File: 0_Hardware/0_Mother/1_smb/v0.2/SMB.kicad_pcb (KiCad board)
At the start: 2 copper layers, 100 x 86 mm, 104 parts, among them IC1 MAX485, IC101 ATMEGA1284-A, IC2 DS2482-100S, J101 RJ45, J102 RTS_RESET, J103 ICSP, J104 SERIAL_REV, J202 USD_CONN, J401 HR911105_RJ45, P1 CONN_2, P101 I2C_CONN, P102 CONN_10X2, P103 CONN_5, P105 CONN_5, P107 CONN_3, P108 CONN_5, P109 CONN_3, P110 CONN_3, P112 CONN_3, P2 CONN_3, P3 CONN_3, P301 CONN_2, P4 CONN_3, P5 CONN_2, Q1 BSS84, SW101 SKQGAKE010, U1 DS1340, U201 ENC28J60, U202 LM1117IMP-3.3, U301 74HC08, U302 MP2562DS, U303 74HC08, X1 CRYSTAL, X101 20MHz, X201 25MHz

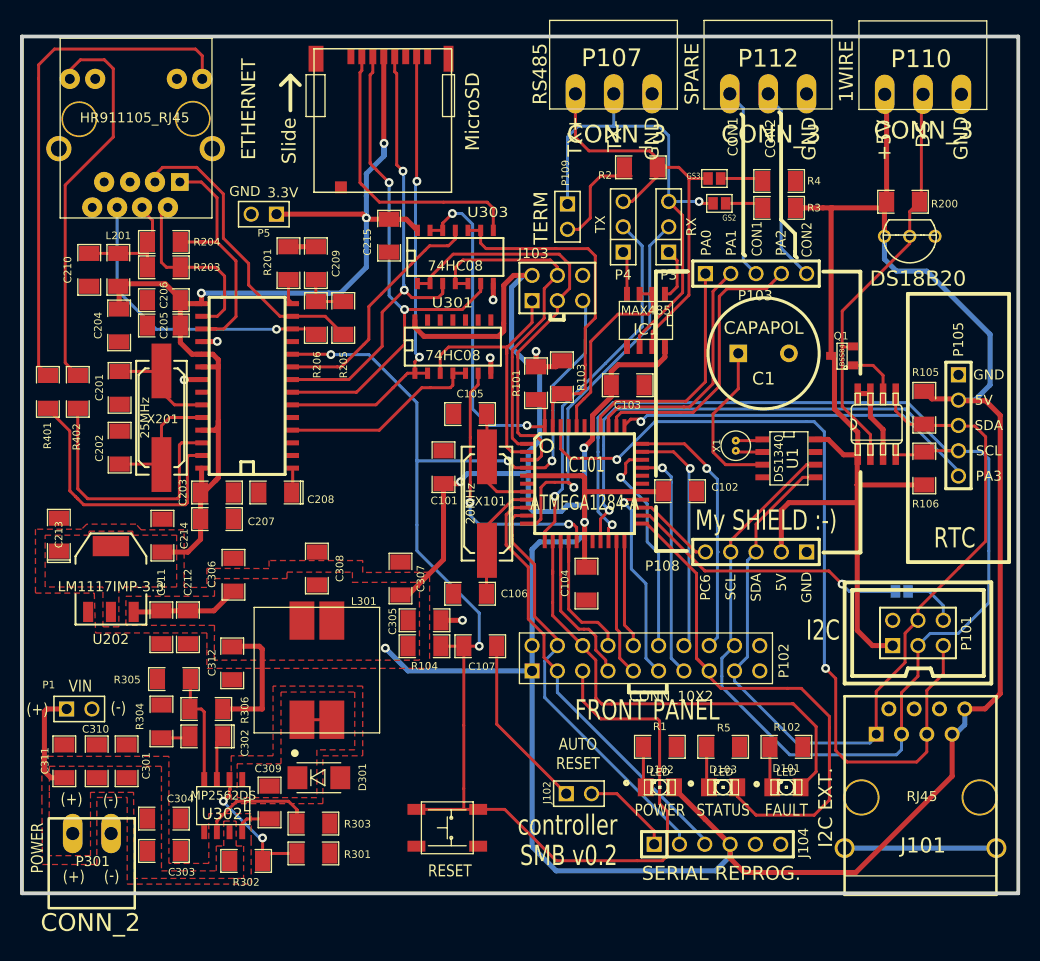
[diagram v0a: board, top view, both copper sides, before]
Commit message: SMB v0.2: remplacement composant mosfet par type P
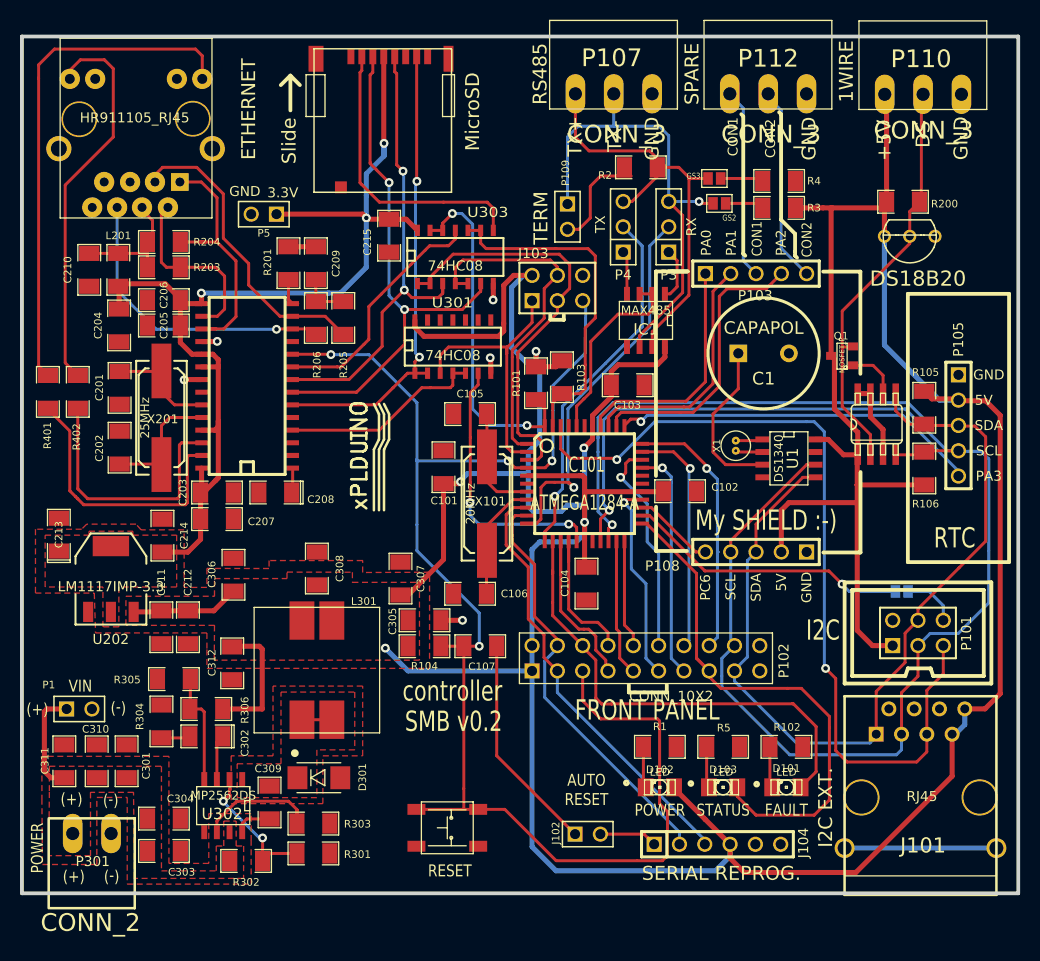
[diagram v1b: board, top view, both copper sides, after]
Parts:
- added logo_xplduino: VAL**, logo_xplduino, F.Cu at (68.6, 69.2)
- Q1: value BSS84 -> MOSFET_P
- moved J102 4.16 mm to (89.8, 107.1)
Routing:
- net N-000004: track 17.7 -> 22.1 mm
- net +5V: track 430.6 -> 426.3 mm
- net N-000003: track 9.17 -> 5.82 mm

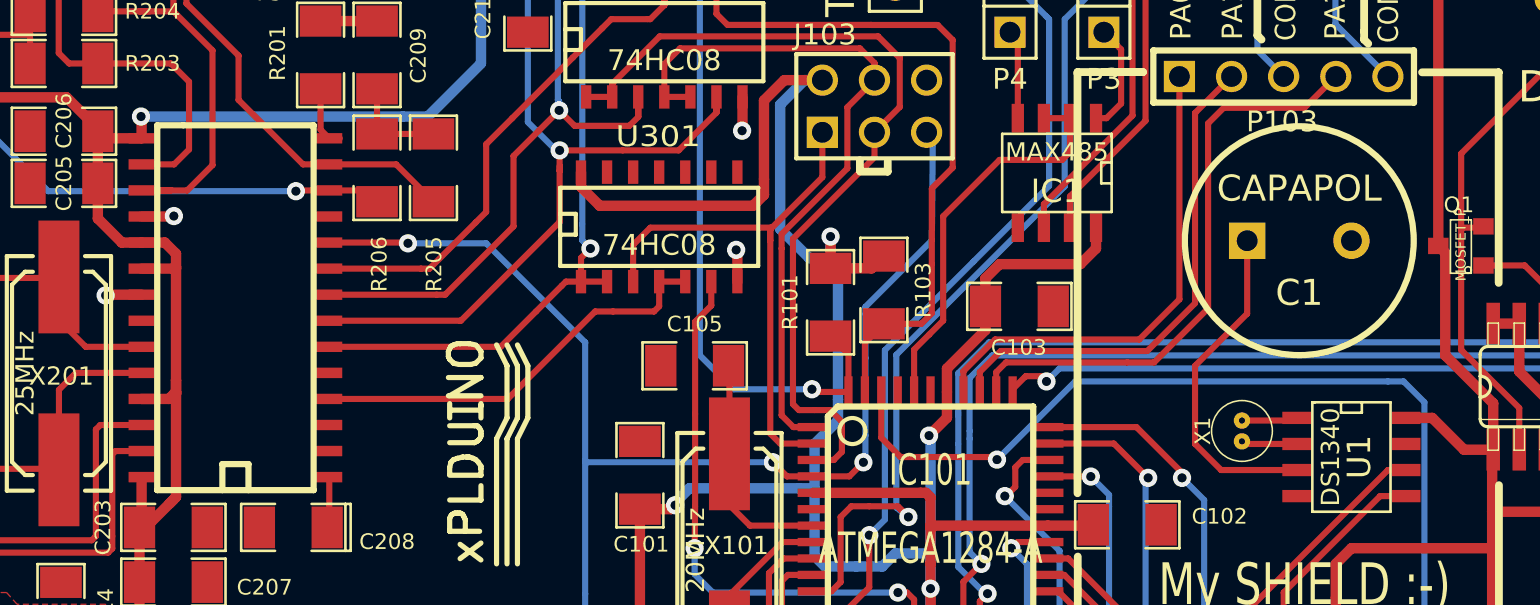
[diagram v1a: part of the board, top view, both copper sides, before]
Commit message: SMB v0.2: descendu de 1mm supercapa car diam 13.5 + U201 nouvel empreinte SOIC-8 (pads allongés pour faciliter soudure)
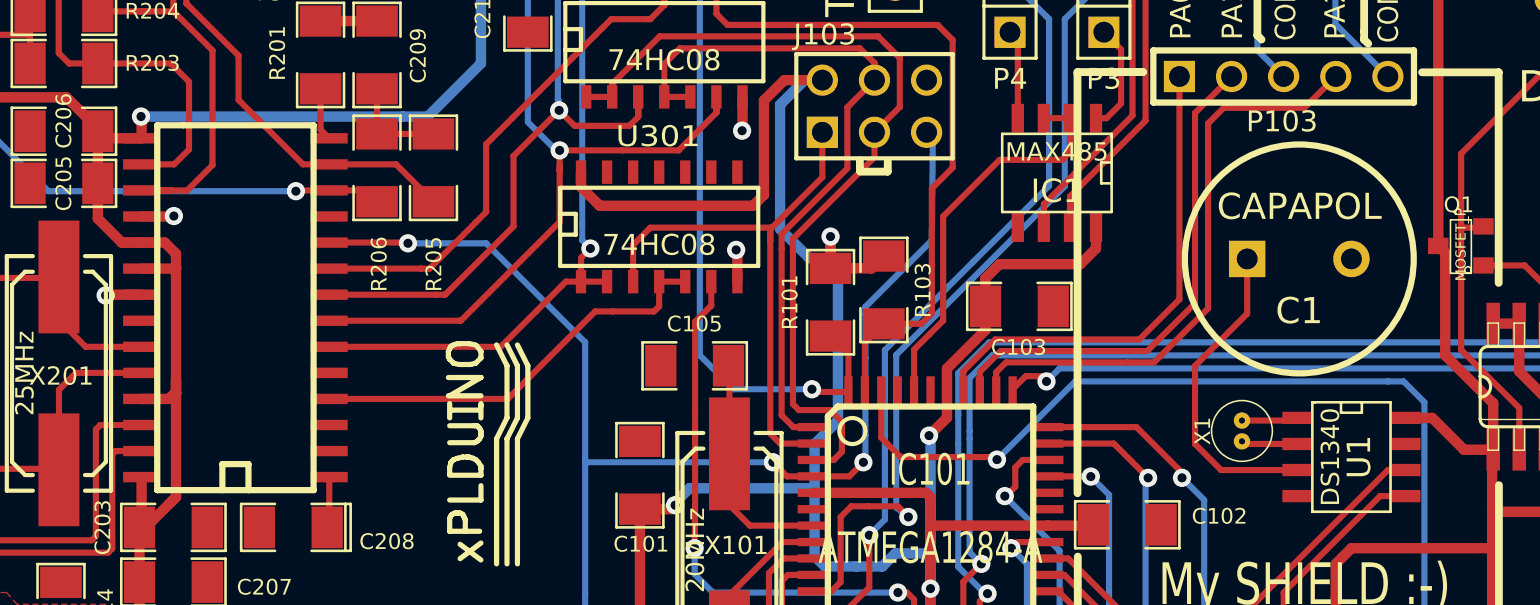
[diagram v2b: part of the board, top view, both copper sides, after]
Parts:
- U201: footprint SO28 -> SO28W
- moved C1 0.89 mm to (107.4, 59.7)
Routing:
- net N-0000022: track 16.4 -> 15.5 mm
